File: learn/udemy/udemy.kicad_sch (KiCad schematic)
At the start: 10 parts

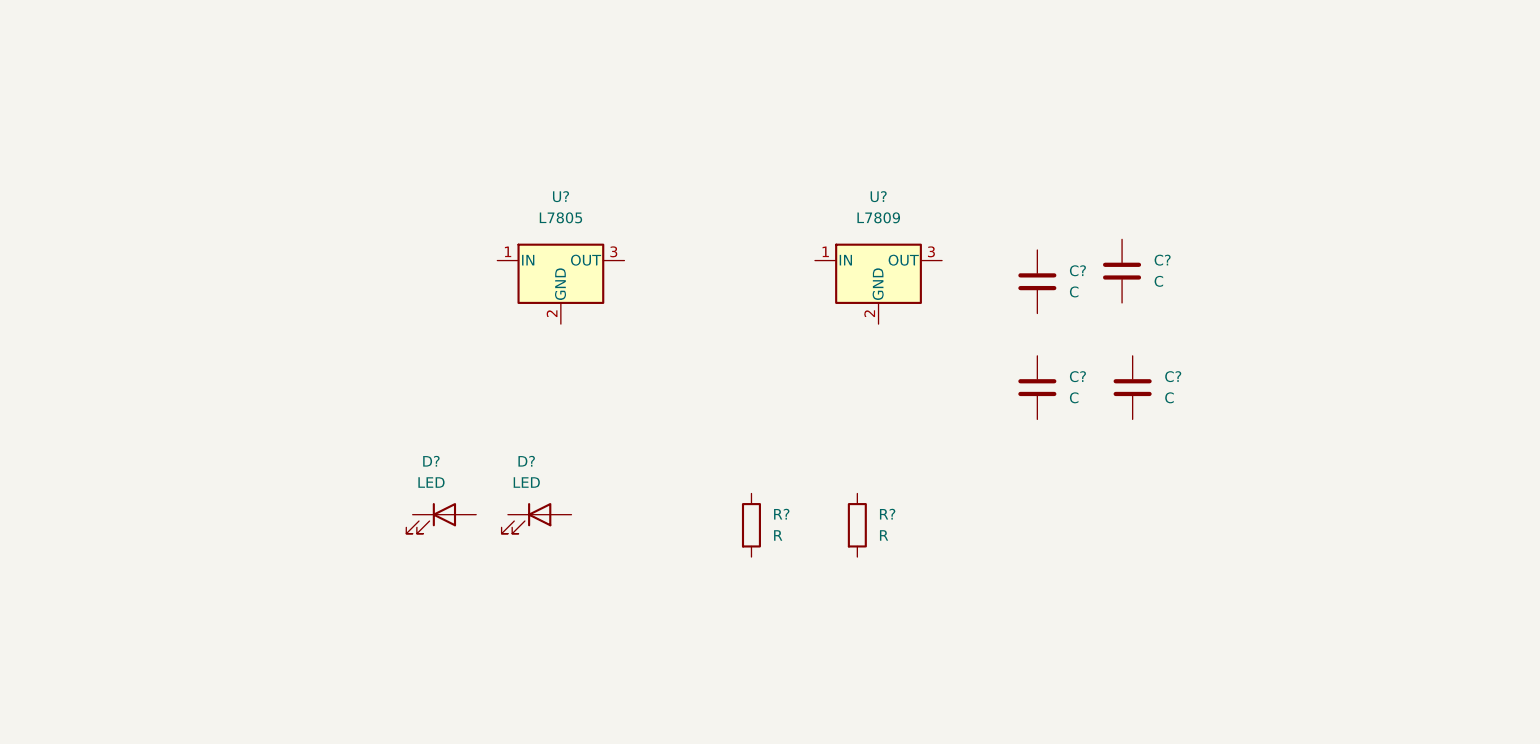
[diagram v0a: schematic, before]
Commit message: 26/12/22 inizio collegamento
Stesura dei primi fili.
(Attenzione, schema non ancora completato)
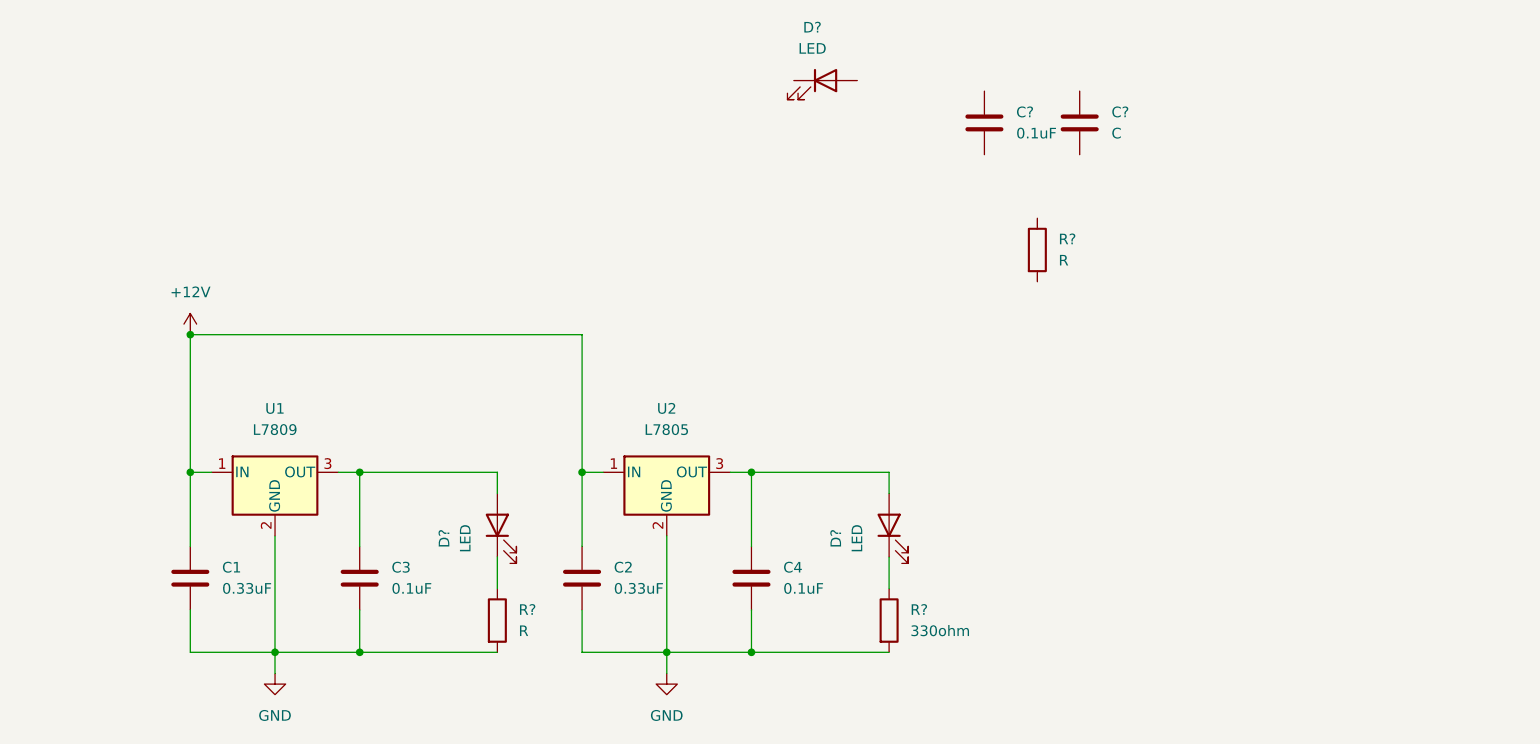
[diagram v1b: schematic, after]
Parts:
- removed C? (x2): C, symbol Device:C
- added C2: 0.33uF, symbol Device:C
- added C4, C?: 0.1uF, symbol Device:C
- added C?: C, symbol Device:C
- added D?: LED, symbol Device:LED
- added R?: 330ohm, symbol Device:R
- C1: renamed from C?; value C -> 0.33uF
- C3: renamed from C?; value C -> 0.1uF
- gave numbers to parts that had none: 2
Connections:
- net +12V: now reaches U1.1 (IN)
- net +12V: now also C1.1, U2.1 (IN), C2.1
- net GND: now reaches U1.2 (GND)
- net GND: now also C1.2, C3.2, R?.2, U2.2 (GND), C2.2, C4.2, R?.2
- net at U1.3 (OUT): now also C3.1, D?.2 (A)
- net at U2.3 (OUT): now also C4.1, D?.2 (A)
- net at R?.1: now also D?.1 (K)
- new net: D?.1 (K), R?.1
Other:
- moved on the sheet: C1, C3, D?, R?, U1, U2

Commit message: 27/12/22 continuazione circuito elettrico
Aggiunto delle nuove componenti e risolto bug.
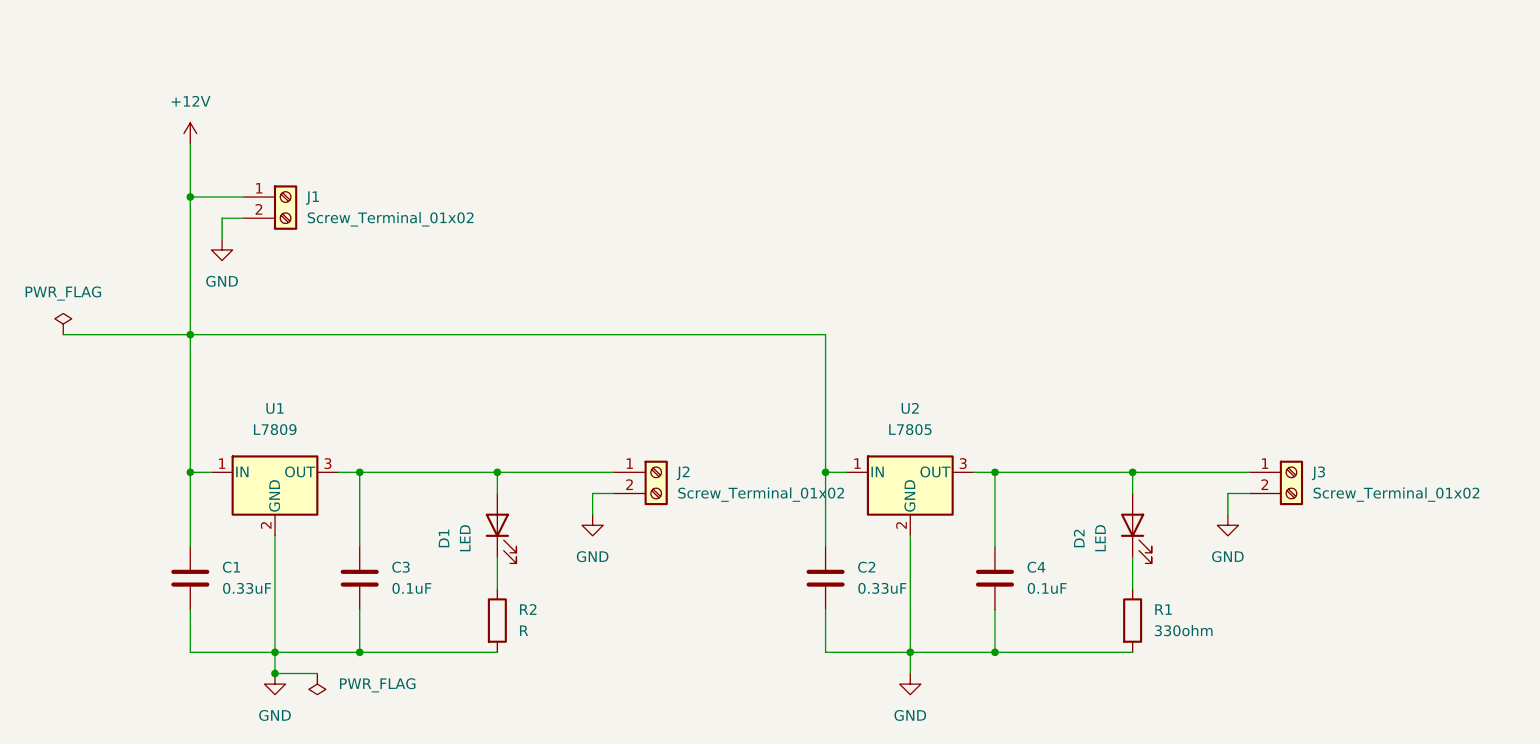
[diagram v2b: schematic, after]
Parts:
- removed C?: 0.1uF, symbol Device:C
- removed C?: C, symbol Device:C
- removed D?: LED, symbol Device:LED
- removed R?: R, symbol Device:R
- added J1, J2, J3: Screw_Terminal_01x02, symbol Connector:Screw_Terminal_01x02
- gave numbers to parts that had none: 4
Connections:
- net +12V: now also J1.1 (Pin_1)
- net GND: now also J1.2 (Pin_2), J2.2 (Pin_2), J3.2 (Pin_2)
- net at C4.1, D2.2 (A), U2.3 (OUT): now also J3.1 (Pin_1)
- net at C3.1, D1.2 (A), U1.3 (OUT): now also J2.1 (Pin_1)
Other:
- moved on the sheet: C2, C4, D2, R1, U2
